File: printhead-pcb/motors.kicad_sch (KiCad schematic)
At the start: 2 parts, among them J12 Cutting_Servo, J13 BlTouch_Servo

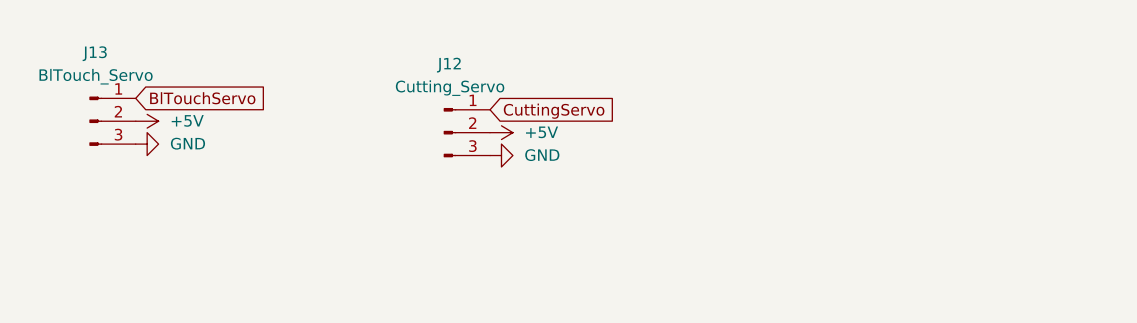
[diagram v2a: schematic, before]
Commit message: Buchse für Netzwerk kabel hinzugefügt, LED Driver überarbeitet, gpio überarbeitet
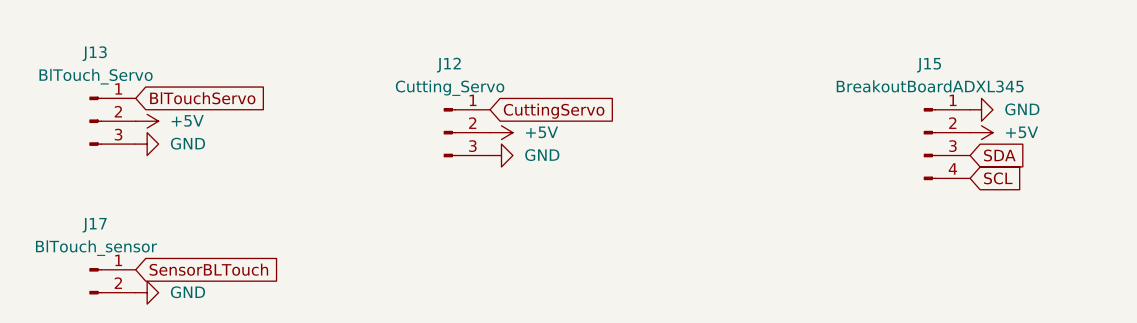
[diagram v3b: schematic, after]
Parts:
- added J15: BreakoutBoardADXL345, Connector_JST:JST_EH_B4B-EH-A_1x04_P2.50mm_Vertical, symbol Connector:Conn_01x04_Pin
- added J17: BlTouch_sensor, Connector_JST:JST_EH_B2B-EH-A_1x02_P2.50mm_Vertical, symbol Connector:Conn_01x02_Pin
- J12, J13: footprint (none) -> Connector_JST:JST_EH_B3B-EH-A_1x03_P2.50mm_Vertical
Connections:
- net +5V: now also J15.2 (Pin_2)
- net GND: now also J15.1 (Pin_1), J17.2 (Pin_2)
- new net SCL: J15.4 (Pin_4)
- new net SDA: J15.3 (Pin_3)
- new net SensorBLTouch: J17.1 (Pin_1)

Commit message: removed led driver, added RJ45 (data connector), fan 3. 4. on off
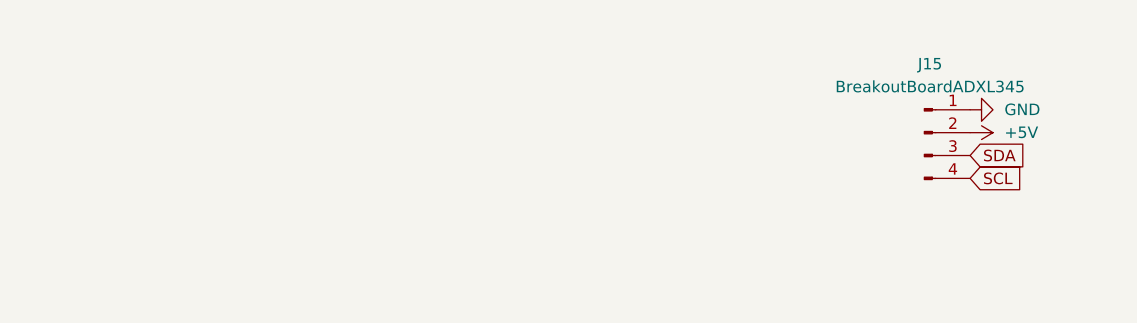
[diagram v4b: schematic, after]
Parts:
- removed J12: Cutting_Servo, Connector_JST:JST_EH_B3B-EH-A_1x03_P2.50mm_Vertical, symbol Connector:Conn_01x03_Pin
- removed J13: BlTouch_Servo, Connector_JST:JST_EH_B3B-EH-A_1x03_P2.50mm_Vertical, symbol Connector:Conn_01x03_Pin
- removed J17: BlTouch_sensor, Connector_JST:JST_EH_B2B-EH-A_1x02_P2.50mm_Vertical, symbol Connector:Conn_01x02_Pin

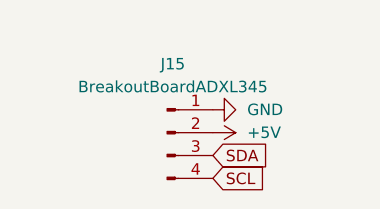
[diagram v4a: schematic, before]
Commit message: Beschriftungen im Schaltplan hinzugefügt
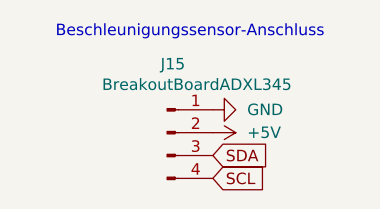
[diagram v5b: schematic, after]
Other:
- note added: "Beschleunigungssensor-Anschluss"
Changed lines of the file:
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@@
 	(generator_version "8.0")
 	(paper "A4")
+	(text "Beschleunigungssensor-Anschluss"
+		(exclude_from_sim no)
+		(at 144.78 38.354 0)
+		(effects
+			(font
+				(size 1.27 1.27)
+			)
+		)
+	)
 	(global_label "SCL"
 		(shape input)
@@
 		)
 		(instances
-			(project ""
+			(project "printhead-pcb"
 				(path "/813ad687-b864-44a5-b729-c4edf26b731d/8c761283-af5f-48de-92da-23f77afbf455"
 					(reference "#PWR028")
@@
 		)
 		(instances
-			(project ""
+			(project "printhead-pcb"
 				(path "/813ad687-b864-44a5-b729-c4edf26b731d/8c761283-af5f-48de-92da-23f77afbf455"
 					(reference "#PWR030")
@@
 		(on_board yes)
 		(dnp no)
-		(fields_autoplaced yes)
 		(property "Reference" "J15"
 			(at 142.875 41.91 0)
@@
 		)
 		(property "Value" "BreakoutBoardADXL345"
-			(at 142.875 44.45 0)
+			(at 145.542 44.196 0)
 			(effects
 				(font
@@
 		)
 		(instances
-			(project ""
+			(project "printhead-pcb"
 				(path "/813ad687-b864-44a5-b729-c4edf26b731d/8c761283-af5f-48de-92da-23f77afbf455"
 					(reference "J15")
